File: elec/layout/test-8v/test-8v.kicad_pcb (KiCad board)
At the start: 2 copper layers, 8 parts, among them U3 10µH ±20%

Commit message: building successfully
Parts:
- R1: value 10kΩ ±1% 62.5mW -> 10.7kΩ ±1% 62.5mW
- R2: value 93.1kΩ ±1% 62.5mW -> 100kΩ ±1% 62.5mW
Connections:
- C2 pad 1: hv-1 -> hv
- C3 pad 1: hv -> hv-1
- R2 pad 1: hv -> hv-1
- U2 pad 4: hv-1 -> hv
- U2 pad 5: hv-1 -> hv
- U3 pad 2: hv -> hv-1
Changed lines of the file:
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@@
             (outputdirectory "")))
     (net 0 "")
-    (net 1 "hv-1")
+    (net 1 "hv")
     (net 2 "gnd-1")
     (net 3 "line")
     (net 4 "CB")
-    (net 5 "hv")
+    (net 5 "hv-1")
     (net 6 "SW")
     (net 7 "gnd")
@@
             (layers "F.Cu" "F.Paste" "F.Mask")
             (remove_unused_layers no)
-            (net 5 "hv"))
+            (net 5 "hv-1"))
         (pad "1" smd rect
             (at -1.6 0 0)
@@
             (layers "F.Cu" "F.Paste" "F.Mask")
             (remove_unused_layers no)
-            (net 1 "hv-1"))
+            (net 1 "hv"))
         (pad "4" smd rect
             (at -1.35 -0.95 0)
@@
             (layers "F.Cu" "F.Paste" "F.Mask")
             (remove_unused_layers no)
-            (net 1 "hv-1"))
+            (net 1 "hv"))
         (model "${KIPRJMOD}/../../../build/footprints/footprints.3dshapes/SOT-23-6_L2.9-W1.6-H1.5-LS2.8-P0.95.step"
             (offset
@@
             (layers "F.Cu" "F.Paste" "F.Mask")
             (remove_unused_layers no)
-            (net 1 "hv-1")))
+            (net 1 "hv")))
     (footprint "atopile:R0402-56259e"
         (layer "F.Cu")
@@
                     (thickness 0.15))
                 (hide no)))
-        (property "Value" "10kΩ ±1% 62.5mW"
+        (property "Value" "10.7kΩ ±1% 62.5mW"
             (at 0 4 0)
             (layer "F.Fab")
@@
                     (size 0.125 0.125)
                     (thickness 0.01875))))
-        (property "LCSC" "C25744"
-            (at 0 0 0)
-            (layer "User.9")
-            (hide yes)
-            (effects
-                (font
-                    (size 0.125 0.125)
-                    (thickness 0.01875))))
-        (property "Partnumber" "0402WGF1002TCE"
+        (property "LCSC" "C270654"
+            (at 0 0 0)
+            (layer "User.9")
+            (hide yes)
+            (effects
+                (font
+                    (size 0.125 0.125)
+                    (thickness 0.01875))))
+        (property "Partnumber" "0402WGF1072TCE"
             (at 0 0 0)
             (layer "User.9")
@@
                     (size 0.125 0.125)
                     (thickness 0.01875))))
-        (property "JLCPCB description" "62.5mW Thick Film Resistors 50V ±100ppm/℃ ±1% 10kΩ 0402 Chip Resistor - Surface Mount ROHS"
+        (property "JLCPCB description" "62.5mW Thick Film Resistors 50V ±100ppm/℃ ±1% 10.7kΩ 0402 Chip Resistor - Surface Mount ROHS"
             (at 0 0 0)
             (layer "User.9")
@@
                     (thickness 0.15))
                 (hide no)))
-        (property "Value" "93.1kΩ ±1% 62.5mW"
+        (property "Value" "100kΩ ±1% 62.5mW"
             (at 0 4 0)
             (layer "F.Fab")
@@
                     (size 0.125 0.125)
                     (thickness 0.01875))))
-        (property "LCSC" "C25925"
-            (at 0 0 0)
-            (layer "User.9")
-            (hide yes)
-            (effects
-                (font
-                    (size 0.125 0.125)
-                    (thickness 0.01875))))
-        (property "Partnumber" "0402WGF9312TCE"
+        (property "LCSC" "C25741"
+            (at 0 0 0)
+            (layer "User.9")
+            (hide yes)
+            (effects
+                (font
+                    (size 0.125 0.125)
+                    (thickness 0.01875))))
+        (property "Partnumber" "0402WGF1003TCE"
             (at 0 0 0)
             (layer "User.9")
@@
                     (size 0.125 0.125)
                     (thickness 0.01875))))
-        (property "JLCPCB description" "62.5mW Thick Film Resistors 50V ±100ppm/℃ ±1% 93.1kΩ 0402 Chip Resistor - Surface Mount ROHS"
+        (property "JLCPCB description" "62.5mW Thick Film Resistors 50V ±100ppm/℃ ±1% 100kΩ 0402 Chip Resistor - Surface Mount ROHS"
             (at 0 0 0)
             (layer "User.9")
@@
             (layers "F.Cu" "F.Paste" "F.Mask")
             (remove_unused_layers no)
-            (net 5 "hv")))
+            (net 5 "hv-1")))
     (footprint "lib:SOD-323_L1.8-W1.3-LS2.5-RD"
         (layer "F.Cu")
@@
             (layers "F.Cu" "F.Paste" "F.Mask")
             (remove_unused_layers no)
-            (net 5 "hv"))))
+            (net 5 "hv-1"))))

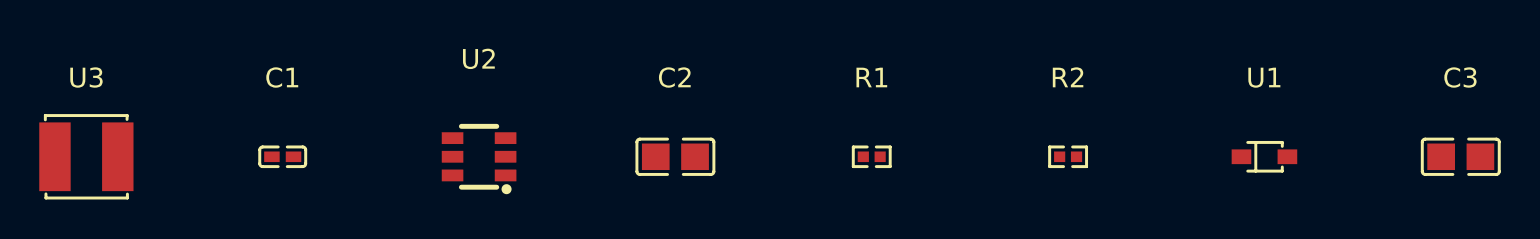
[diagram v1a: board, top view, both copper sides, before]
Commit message: Update layouts to kicad 9, add default build for layout reuse
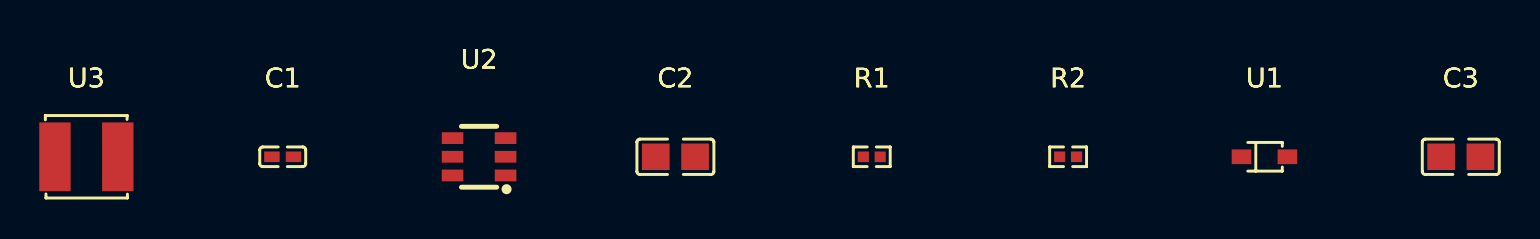
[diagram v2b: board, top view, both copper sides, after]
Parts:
- C2: value 10µF ±10% 25V X5R -> 4.7µF ±10% 25V X5R
- R1: value 10.7kΩ ±1% 62.5mW -> 10kΩ ±1% 62.5mW
- R2: value 100kΩ ±1% 62.5mW -> 93.1kΩ ±1% 62.5mW
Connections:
- net line renamed FB
